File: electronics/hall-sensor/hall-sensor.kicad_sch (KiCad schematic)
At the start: 9 parts, among them J1 Conn_01x03, U1 DRV5033AJQLPGM

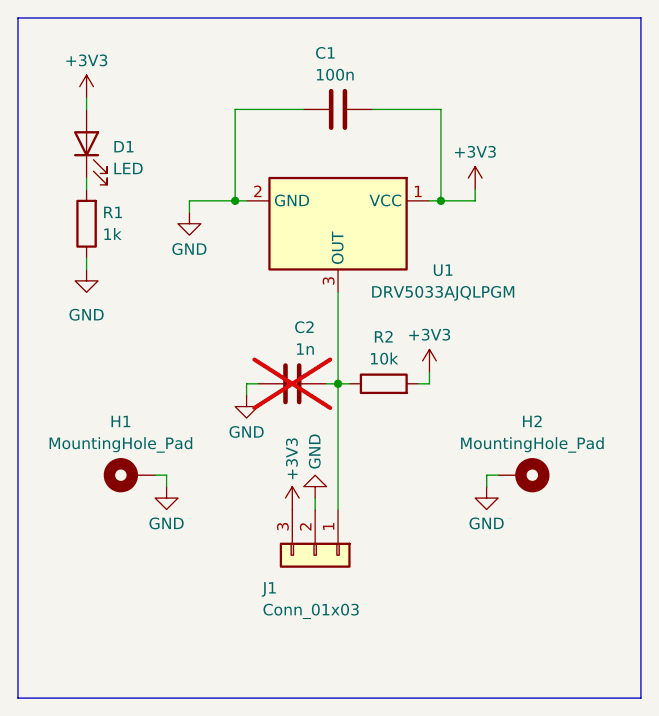
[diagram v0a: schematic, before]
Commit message: voltage divider added for output pin of hall sensor
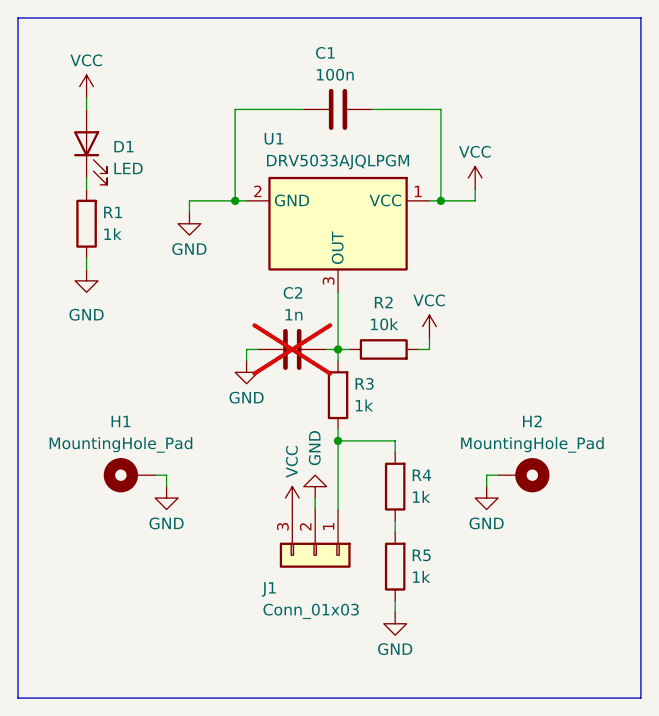
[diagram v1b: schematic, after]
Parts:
- added R3, R4, R5: 1k, Resistor_SMD:R_0805_2012Metric, symbol Device:R
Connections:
- net GND: now also R5.1
- net at C2.2, R2.1, U1.3 (OUT): now also R3.2; no longer J1.1 (Pin_1)
- net +3V3 renamed VCC
- new net: J1.1 (Pin_1), R3.1, R4.2
- new net: R4.1, R5.2
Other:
- moved on the sheet: C2, R2
